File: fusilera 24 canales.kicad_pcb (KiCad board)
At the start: 4 copper layers, 53 parts, among them J1 +12V borne M6, J2 GND borne M5, Q1 MMBT2222A, Q2 MMBT2222A, U1 LM339D, U2 74HC132D, U3 BTS50010-1TAD, U4 MCP23017-E/SO, U5 MCP23017-E/SO, U6 LM5164DDA, U7 AP2112K-3.3

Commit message: Convierte los canales en una hoja jerárquica de celda con dos instancias
- Nueva hoja celda4.kicad_sch (4 canales, 1 LM339 y 2 × 74HC132) instanciada
  como Celda1 y Celda2 en la hoja principal; las referencias de la Celda2 son
  las de la Celda1 más 100.
- Etiquetas únicas por canal como pines de hoja (ESP32_OUT1-4, MANUAL1-4,
  OUT1-4, FALLA1-4): ya no se unen entre sí las salidas, las entradas ni las
  fallas de distintos canales.
- Añade los pull-ups de 10 k que faltaban en las salidas de los comparadores de
  los canales 3 y 4 (R53 y R54).
- Re-vincula en el PCB los 25 footprints existentes de la celda a la Celda1 para
  conservar su colocación.
- La huella de la ESP32 lleva los nombres de los pines en la serigrafía.
- CONTEXTO_PROYECTO.md actualizado: 28 canales (19 controlados y 9 siempre en
  alto), reparto de E/S sin tercer MCP y estructura jerárquica.
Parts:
- added C101: 100uF 16V, Capacitor_SMD:CP_Elec_6.3x5.4, F.Cu at (42.5, 148.8)
- added C102: 100nF, Capacitor_SMD:C_0805_2012Metric, F.Cu at (72.4, 130.0)
- added C103: 1uF 25V, Capacitor_SMD:CP_Elec_4x5.4, F.Cu at (41.1, 102.2)
- added C104: 100nF, Capacitor_SMD:C_0805_2012Metric, F.Cu at (72.4, 133.0)
- added C105: 1uF 25V, Capacitor_SMD:CP_Elec_4x5.4, F.Cu at (41.1, 108.0)
- added C116: 1uF 25V, Capacitor_SMD:CP_Elec_4x5.4, F.Cu at (41.1, 113.9)
- added C117: 1uF 25V, Capacitor_SMD:CP_Elec_4x5.4, F.Cu at (41.1, 119.7)
- added C118: 1uF 25V, Capacitor_SMD:CP_Elec_4x5.4, F.Cu at (41.1, 125.6)
- added C119: 1uF 25V, Capacitor_SMD:CP_Elec_4x5.4, F.Cu at (48.8, 102.2)
- added C120: 100nF, Capacitor_SMD:C_0805_2012Metric, F.Cu at (72.4, 136.0)
- added C121: 1uF 25V, Capacitor_SMD:CP_Elec_4x5.4, F.Cu at (48.8, 108.0)
- added C122: 1uF 25V, Capacitor_SMD:CP_Elec_4x5.4, F.Cu at (48.8, 113.9)
- added C16: 1uF 25V, Capacitor_SMD:CP_Elec_4x5.4, F.Cu at (41.1, 157.8)
- added C17: 1uF 25V, Capacitor_SMD:CP_Elec_4x5.4, F.Cu at (41.1, 163.6)
- added C18: 1uF 25V, Capacitor_SMD:CP_Elec_4x5.4, F.Cu at (41.1, 169.5)
- added C19: 1uF 25V, Capacitor_SMD:CP_Elec_4x5.4, F.Cu at (41.1, 175.3)
- added C20: 100nF, Capacitor_SMD:C_0805_2012Metric, F.Cu at (47.2, 196.3)
- added C21: 1uF 25V, Capacitor_SMD:CP_Elec_4x5.4, F.Cu at (41.1, 181.2)
- added C22: 1uF 25V, Capacitor_SMD:CP_Elec_4x5.4, F.Cu at (41.1, 187.0)
- added D10: LED rojo, LED_SMD:LED_0805_2012Metric, F.Cu at (64.8, 162.4)
- added D101: BAT54C, Package_TO_SOT_SMD:SOT-23, F.Cu at (53.0, 130.7)
- added D102: LED verde, LED_SMD:LED_0805_2012Metric, F.Cu at (77.0, 100.8)
- added D103: LED rojo, LED_SMD:LED_0805_2012Metric, F.Cu at (77.0, 103.8)
- added D107: LED verde, LED_SMD:LED_0805_2012Metric, F.Cu at (77.0, 106.8)
- added D108: BAT54C, Package_TO_SOT_SMD:SOT-23, F.Cu at (53.0, 135.2)
- added D109: LED rojo, LED_SMD:LED_0805_2012Metric, F.Cu at (77.0, 109.9)
- added D11: LED rojo, LED_SMD:LED_0805_2012Metric, F.Cu at (64.8, 165.5)
- added D110: LED rojo, LED_SMD:LED_0805_2012Metric, F.Cu at (77.0, 112.9)
- added D111: LED rojo, LED_SMD:LED_0805_2012Metric, F.Cu at (77.0, 116.0)
- added D112: LED verde, LED_SMD:LED_0805_2012Metric, F.Cu at (77.0, 119.0)
- added D113: LED verde, LED_SMD:LED_0805_2012Metric, F.Cu at (77.0, 122.0)
- added D114: BAT54C, Package_TO_SOT_SMD:SOT-23, F.Cu at (53.0, 139.6)
- added D115: BAT54C, Package_TO_SOT_SMD:SOT-23, F.Cu at (57.9, 130.7)
- added D12: LED verde, LED_SMD:LED_0805_2012Metric, F.Cu at (64.8, 168.5)
- added D13: LED verde, LED_SMD:LED_0805_2012Metric, F.Cu at (64.8, 171.6)
- added D14: BAT54C, Package_TO_SOT_SMD:SOT-23, F.Cu at (47.4, 188.1)
- added D15: BAT54C, Package_TO_SOT_SMD:SOT-23, F.Cu at (47.4, 192.5)
- added D7: LED verde, LED_SMD:LED_0805_2012Metric, F.Cu at (64.8, 156.4)
- added D8: BAT54C, Package_TO_SOT_SMD:SOT-23, F.Cu at (47.4, 183.6)
- added D9: LED rojo, LED_SMD:LED_0805_2012Metric, F.Cu at (64.8, 159.4)
- added Q101: MMBT2222A, Package_TO_SOT_SMD:SOT-23, F.Cu at (57.9, 135.2)
- added Q102: MMBT2222A, Package_TO_SOT_SMD:SOT-23, F.Cu at (57.9, 139.6)
- added Q103: MMBT2222A, Package_TO_SOT_SMD:SOT-23, F.Cu at (62.8, 130.7)
- added Q104: MMBT2222A, Package_TO_SOT_SMD:SOT-23, F.Cu at (62.8, 135.2)
- added Q105: MMBT2222A, Package_TO_SOT_SMD:SOT-23, F.Cu at (62.8, 139.6)
- added Q106: MMBT2222A, Package_TO_SOT_SMD:SOT-23, F.Cu at (67.7, 130.7)
- added Q107: MMBT2222A, Package_TO_SOT_SMD:SOT-23, F.Cu at (67.7, 135.2)
- added Q108: MMBT2222A, Package_TO_SOT_SMD:SOT-23, F.Cu at (67.7, 139.6)
- added Q3: MMBT2222A, Package_TO_SOT_SMD:SOT-23, F.Cu at (52.3, 183.6)
- added Q4: MMBT2222A, Package_TO_SOT_SMD:SOT-23, F.Cu at (52.3, 188.1)
- added Q5: MMBT2222A, Package_TO_SOT_SMD:SOT-23, F.Cu at (52.3, 192.5)
- added Q6: MMBT2222A, Package_TO_SOT_SMD:SOT-23, F.Cu at (57.2, 183.6)
- added Q7: MMBT2222A, Package_TO_SOT_SMD:SOT-23, F.Cu at (57.2, 188.1)
- added Q8: MMBT2222A, Package_TO_SOT_SMD:SOT-23, F.Cu at (57.2, 192.5)
- added R101: umbral, Resistor_THT:R_Axial_DIN0207_L6.3mm_D2.5mm_P10.16mm_Horizontal, F.Cu at (38.8, 130.5)
- added R102: 10k, Resistor_SMD:R_0805_2012Metric, F.Cu at (54.9, 100.7)
- added R103: 10k, Resistor_SMD:R_0805_2012Metric, F.Cu at (54.9, 103.7)
- added R104: 4.7k, Resistor_SMD:R_0805_2012Metric, F.Cu at (54.9, 106.6)
- added R105: 4.7k, Resistor_SMD:R_0805_2012Metric, F.Cu at (54.9, 109.6)
- added R106: 10k, Resistor_SMD:R_0805_2012Metric, F.Cu at (54.9, 112.5)
- added R107: 100k, Resistor_SMD:R_0805_2012Metric, F.Cu at (54.9, 115.5)
- added R108: 100k, Resistor_SMD:R_0805_2012Metric, F.Cu at (54.9, 118.4)
- added R109: 1k, Resistor_SMD:R_0805_2012Metric, F.Cu at (54.9, 121.4)
- added R110: 2.2k, Resistor_SMD:R_0805_2012Metric, F.Cu at (54.9, 124.3)
- added R111: 4.7k, Resistor_SMD:R_0805_2012Metric, F.Cu at (59.3, 100.7)
- added R112: 1k, Resistor_SMD:R_0805_2012Metric, F.Cu at (59.3, 103.7)
- added R119: 4.7k, Resistor_SMD:R_0805_2012Metric, F.Cu at (59.3, 106.6)
- added R120: 4.7k, Resistor_SMD:R_0805_2012Metric, F.Cu at (59.3, 109.6)
- added R121: 2.2k, Resistor_SMD:R_0805_2012Metric, F.Cu at (59.3, 112.5)
- added R122: 100k, Resistor_SMD:R_0805_2012Metric, F.Cu at (59.3, 115.5)
- added R123: 100k, Resistor_SMD:R_0805_2012Metric, F.Cu at (59.3, 118.4)
- added R124: 1k, Resistor_SMD:R_0805_2012Metric, F.Cu at (59.3, 121.4)
- added R125: 1k, Resistor_SMD:R_0805_2012Metric, F.Cu at (59.3, 124.3)
- added R126: 4.7k, Resistor_SMD:R_0805_2012Metric, F.Cu at (63.7, 100.7)
- added R127: 10k, Resistor_SMD:R_0805_2012Metric, F.Cu at (63.7, 103.7)
- added R128: 10k, Resistor_SMD:R_0805_2012Metric, F.Cu at (63.7, 106.6)
- added R129: umbral, Resistor_THT:R_Axial_DIN0207_L6.3mm_D2.5mm_P10.16mm_Horizontal, F.Cu at (38.8, 134.6)
- added R130: 10k, Resistor_SMD:R_0805_2012Metric, F.Cu at (63.7, 109.6)
- added R131: 10k, Resistor_SMD:R_0805_2012Metric, F.Cu at (63.7, 112.5)
- added R132: 10k, Resistor_SMD:R_0805_2012Metric, F.Cu at (63.7, 115.5)
- added R133: 1k, Resistor_SMD:R_0805_2012Metric, F.Cu at (63.7, 118.4)
- added R134: 1k, Resistor_SMD:R_0805_2012Metric, F.Cu at (63.7, 121.4)
- added R135: 4.7k, Resistor_SMD:R_0805_2012Metric, F.Cu at (63.7, 124.3)
- added R136: 4.7k, Resistor_SMD:R_0805_2012Metric, F.Cu at (68.1, 100.7)
- added R137: 4.7k, Resistor_SMD:R_0805_2012Metric, F.Cu at (68.1, 103.7)
- added R138: 4.7k, Resistor_SMD:R_0805_2012Metric, F.Cu at (68.1, 106.6)
- added R139: 4.7k, Resistor_SMD:R_0805_2012Metric, F.Cu at (68.1, 109.6)
- added R140: 4.7k, Resistor_SMD:R_0805_2012Metric, F.Cu at (68.1, 112.5)
- added R141: 2.2k, Resistor_SMD:R_0805_2012Metric, F.Cu at (68.1, 115.5)
- added R142: 2.2k, Resistor_SMD:R_0805_2012Metric, F.Cu at (68.1, 118.4)
- added R143: 100k, Resistor_SMD:R_0805_2012Metric, F.Cu at (68.1, 121.4)
- added R144: 100k, Resistor_SMD:R_0805_2012Metric, F.Cu at (68.1, 124.3)
- added R145: 100k, Resistor_SMD:R_0805_2012Metric, F.Cu at (72.5, 100.7)
- added R146: 100k, Resistor_SMD:R_0805_2012Metric, F.Cu at (72.5, 103.7)
- added R147: 1k, Resistor_SMD:R_0805_2012Metric, F.Cu at (72.5, 106.6)
- added R148: 1k, Resistor_SMD:R_0805_2012Metric, F.Cu at (72.5, 109.6)
- added R149: umbral, Resistor_THT:R_Axial_DIN0207_L6.3mm_D2.5mm_P10.16mm_Horizontal, F.Cu at (38.8, 138.6)
- added R150: 10k, Resistor_SMD:R_0805_2012Metric, F.Cu at (72.5, 112.5)
- added R151: umbral, Resistor_THT:R_Axial_DIN0207_L6.3mm_D2.5mm_P10.16mm_Horizontal, F.Cu at (38.8, 142.7)
- added R152: 10k, Resistor_SMD:R_0805_2012Metric, F.Cu at (72.5, 115.5)
- added R153: 10k, Resistor_SMD:R_0805_2012Metric, F.Cu at (72.5, 118.4)
- added R154: 10k, Resistor_SMD:R_0805_2012Metric, F.Cu at (72.5, 121.4)
- added R19: 4.7k, Resistor_SMD:R_0805_2012Metric, F.Cu at (47.2, 156.3)
- added R20: 4.7k, Resistor_SMD:R_0805_2012Metric, F.Cu at (47.2, 159.3)
- added R21: 2.2k, Resistor_SMD:R_0805_2012Metric, F.Cu at (47.2, 162.2)
- added R22: 100k, Resistor_SMD:R_0805_2012Metric, F.Cu at (47.2, 165.2)
- added R23: 100k, Resistor_SMD:R_0805_2012Metric, F.Cu at (47.2, 168.1)
- added R24: 1k, Resistor_SMD:R_0805_2012Metric, F.Cu at (47.2, 171.1)
- added R25: 1k, Resistor_SMD:R_0805_2012Metric, F.Cu at (47.2, 174.0)
- added R26: 4.7k, Resistor_SMD:R_0805_2012Metric, F.Cu at (47.2, 177.0)
- added R27: 10k, Resistor_SMD:R_0805_2012Metric, F.Cu at (47.2, 179.9)
- added R28: 10k, Resistor_SMD:R_0805_2012Metric, F.Cu at (51.6, 156.3)
- added R29: umbral, Resistor_THT:R_Axial_DIN0207_L6.3mm_D2.5mm_P10.16mm_Horizontal, F.Cu at (21.1, 193.9)
- added R30: 10k, Resistor_SMD:R_0805_2012Metric, F.Cu at (51.6, 159.3)
- added R31: 10k, Resistor_SMD:R_0805_2012Metric, F.Cu at (51.6, 162.2)
- added R32: 10k, Resistor_SMD:R_0805_2012Metric, F.Cu at (51.6, 165.2)
- added R33: 1k, Resistor_SMD:R_0805_2012Metric, F.Cu at (51.6, 168.1)
- added R34: 1k, Resistor_SMD:R_0805_2012Metric, F.Cu at (51.6, 171.1)
- added R35: 4.7k, Resistor_SMD:R_0805_2012Metric, F.Cu at (51.6, 174.0)
- added R36: 4.7k, Resistor_SMD:R_0805_2012Metric, F.Cu at (51.6, 177.0)
- added R37: 4.7k, Resistor_SMD:R_0805_2012Metric, F.Cu at (51.6, 179.9)
- added R38: 4.7k, Resistor_SMD:R_0805_2012Metric, F.Cu at (56.0, 156.3)
- added R39: 4.7k, Resistor_SMD:R_0805_2012Metric, F.Cu at (56.0, 159.3)
- added R40: 4.7k, Resistor_SMD:R_0805_2012Metric, F.Cu at (56.0, 162.2)
- added R41: 2.2k, Resistor_SMD:R_0805_2012Metric, F.Cu at (56.0, 165.2)
- added R42: 2.2k, Resistor_SMD:R_0805_2012Metric, F.Cu at (56.0, 168.1)
- added R43: 100k, Resistor_SMD:R_0805_2012Metric, F.Cu at (56.0, 171.1)
- added R44: 100k, Resistor_SMD:R_0805_2012Metric, F.Cu at (56.0, 174.0)
- added R45: 100k, Resistor_SMD:R_0805_2012Metric, F.Cu at (56.0, 177.0)
- added R46: 100k, Resistor_SMD:R_0805_2012Metric, F.Cu at (56.0, 179.9)
- added R47: 1k, Resistor_SMD:R_0805_2012Metric, F.Cu at (60.4, 156.3)
- added R48: 1k, Resistor_SMD:R_0805_2012Metric, F.Cu at (60.4, 159.3)
- added R49: umbral, Resistor_THT:R_Axial_DIN0207_L6.3mm_D2.5mm_P10.16mm_Horizontal, F.Cu at (21.1, 198.0)
- added R50: 10k, Resistor_SMD:R_0805_2012Metric, F.Cu at (60.4, 162.2)
- added R51: umbral, Resistor_THT:R_Axial_DIN0207_L6.3mm_D2.5mm_P10.16mm_Horizontal, F.Cu at (21.1, 202.0)
- added R52: 10k, Resistor_SMD:R_0805_2012Metric, F.Cu at (60.4, 165.2)
- added R53: 10k, Resistor_SMD:R_0805_2012Metric, F.Cu at (60.4, 168.1)
- added R54: 10k, Resistor_SMD:R_0805_2012Metric, F.Cu at (60.4, 171.1)
- added U10: BTS50010-1TAD, Package_TO_SOT_SMD:TO-263-7_TabPin4, F.Cu at (30.2, 173.4)
- added U101: LM339D, Package_SO:SOIC-14_3.9x8.7mm_P1.27mm, F.Cu at (54.7, 147.1)
- added U102: 74HC132D, Package_SO:SOIC-14_3.9x8.7mm_P1.27mm, F.Cu at (63.2, 147.1)
- added U103: BTS50010-1TAD, Package_TO_SOT_SMD:TO-263-7_TabPin4, F.Cu at (30.2, 105.4)
- added U108: BTS50010-1TAD, Package_TO_SOT_SMD:TO-263-7_TabPin4, F.Cu at (30.2, 117.8)
- added U109: 74HC132D, Package_SO:SOIC-14_3.9x8.7mm_P1.27mm, F.Cu at (71.6, 147.1)
- added U11: BTS50010-1TAD, Package_TO_SOT_SMD:TO-263-7_TabPin4, F.Cu at (30.2, 185.7)
- added U110: BTS50010-1TAD, Package_TO_SOT_SMD:TO-263-7_TabPin4, F.Cu at (30.2, 130.1)
- added U111: BTS50010-1TAD, Package_TO_SOT_SMD:TO-263-7_TabPin4, F.Cu at (30.2, 142.5)
- added U8: BTS50010-1TAD, Package_TO_SOT_SMD:TO-263-7_TabPin4, F.Cu at (30.2, 161.0)
- added U9: 74HC132D, Package_SO:SOIC-14_3.9x8.7mm_P1.27mm, F.Cu at (63.9, 186.7)
- moved A1 110.6 mm to (121.8, 63.0)
- moved U3 82.2 mm to (184.7, 63.7)
- moved R1 53.5 mm to (15.2, 32.0)
- moved U1 29.9 mm to (34.8, 34.5)
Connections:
- net /ESP32 OUT renamed /Celda1/ESP32_OUT1
- net /MANUAL renamed /Celda1/MANUAL1
- net /OUT renamed /Celda1/OUT1
- net /U2A-3 renamed Net-(U2-Pad3)
- net U2A-2 renamed /Celda1/FALLA1
- net U2B-4 renamed Net-(R3-Pad1)
- net U3-IN renamed Net-(Q2-C)
- net U3-IS renamed Net-(U1A--)
- U1 pad 1: unconnected-(U1-Pad1) -> Net-(R27-Pad1)
- U1 pad 10: unconnected-(U1C---Pad10) -> Net-(U10-IS)
- U1 pad 11: unconnected-(U1C-+-Pad11) -> Net-(U1C-+)
- U1 pad 13: unconnected-(U1-Pad13) -> Net-(R53-Pad1)
- U1 pad 14: unconnected-(U1-Pad14) -> Net-(R54-Pad1)
- U1 pad 6: unconnected-(U1B---Pad6) -> Net-(U1B--)
- U1 pad 7: unconnected-(U1B-+-Pad7) -> Net-(U1B-+)
- U1 pad 8: unconnected-(U1D---Pad8) -> Net-(U11-IS)
- U1 pad 9: unconnected-(U1D-+-Pad9) -> Net-(U1D-+)
- U2 pad 10: unconnected-(U2-Pad10) -> /Celda1/FALLA2
- U2 pad 11: unconnected-(U2-Pad11) -> /Celda1/FALLA2
- U2 pad 12: unconnected-(U2-Pad12) -> Net-(R27-Pad1)
- U2 pad 13: unconnected-(U2-Pad13) -> Net-(U2-Pad13)
- U2 pad 8: unconnected-(U2-Pad8) -> Net-(U2-Pad13)
- U2 pad 9: unconnected-(U2-Pad9) -> Net-(C17-Pad1)

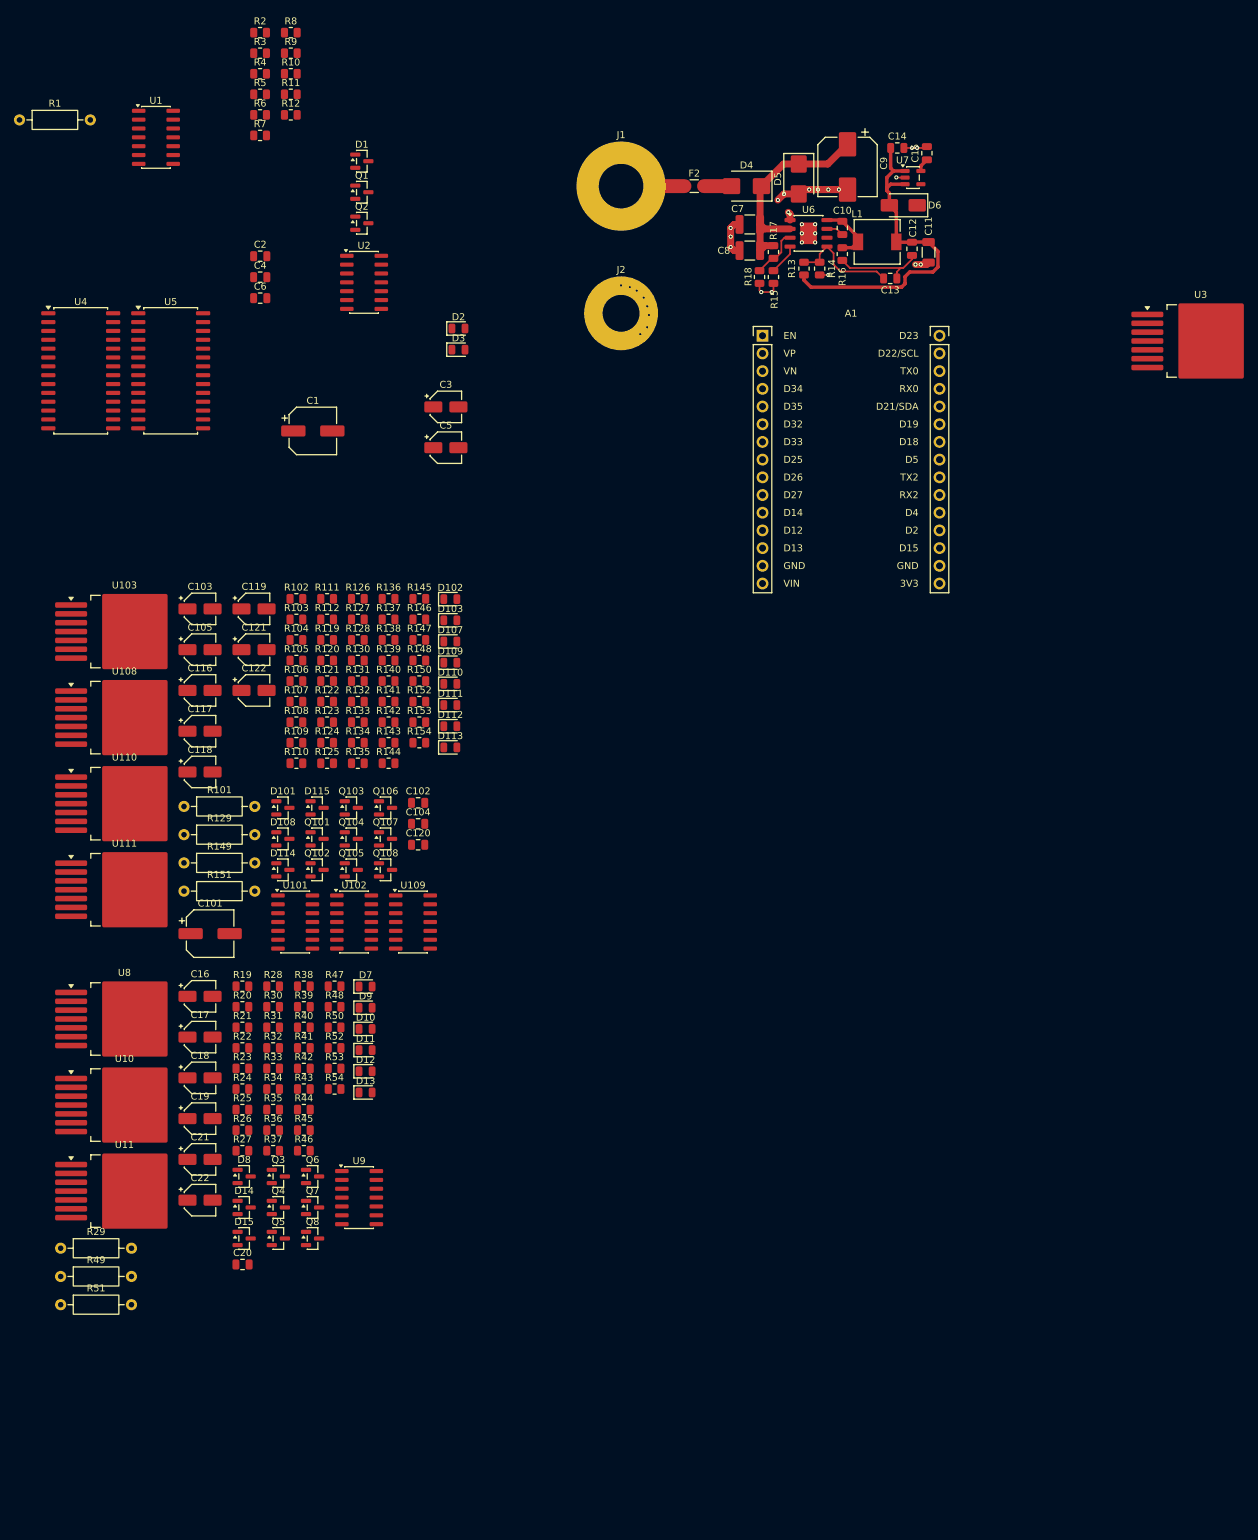
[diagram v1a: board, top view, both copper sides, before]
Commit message: Importa las dos celdas al PCB y avanza el ruteo de la Celda1
- Importa a la placa los 202 footprints (bloque de alimentación, ESP32, MCP23017
  y las celdas Celda1 y Celda2); paridad con el esquemático sin problemas.
- Avanza el ruteo: 371 segmentos y 43 vías; el plano de GND de In1 se mantiene.
- Reubica en el esquemático el grupo del ESP32 y los MCP23017.
- El DRC sigue marcando el contorno que falta, 260 conexiones por rutear y
  18 avisos de espaciado pendientes de revisar.
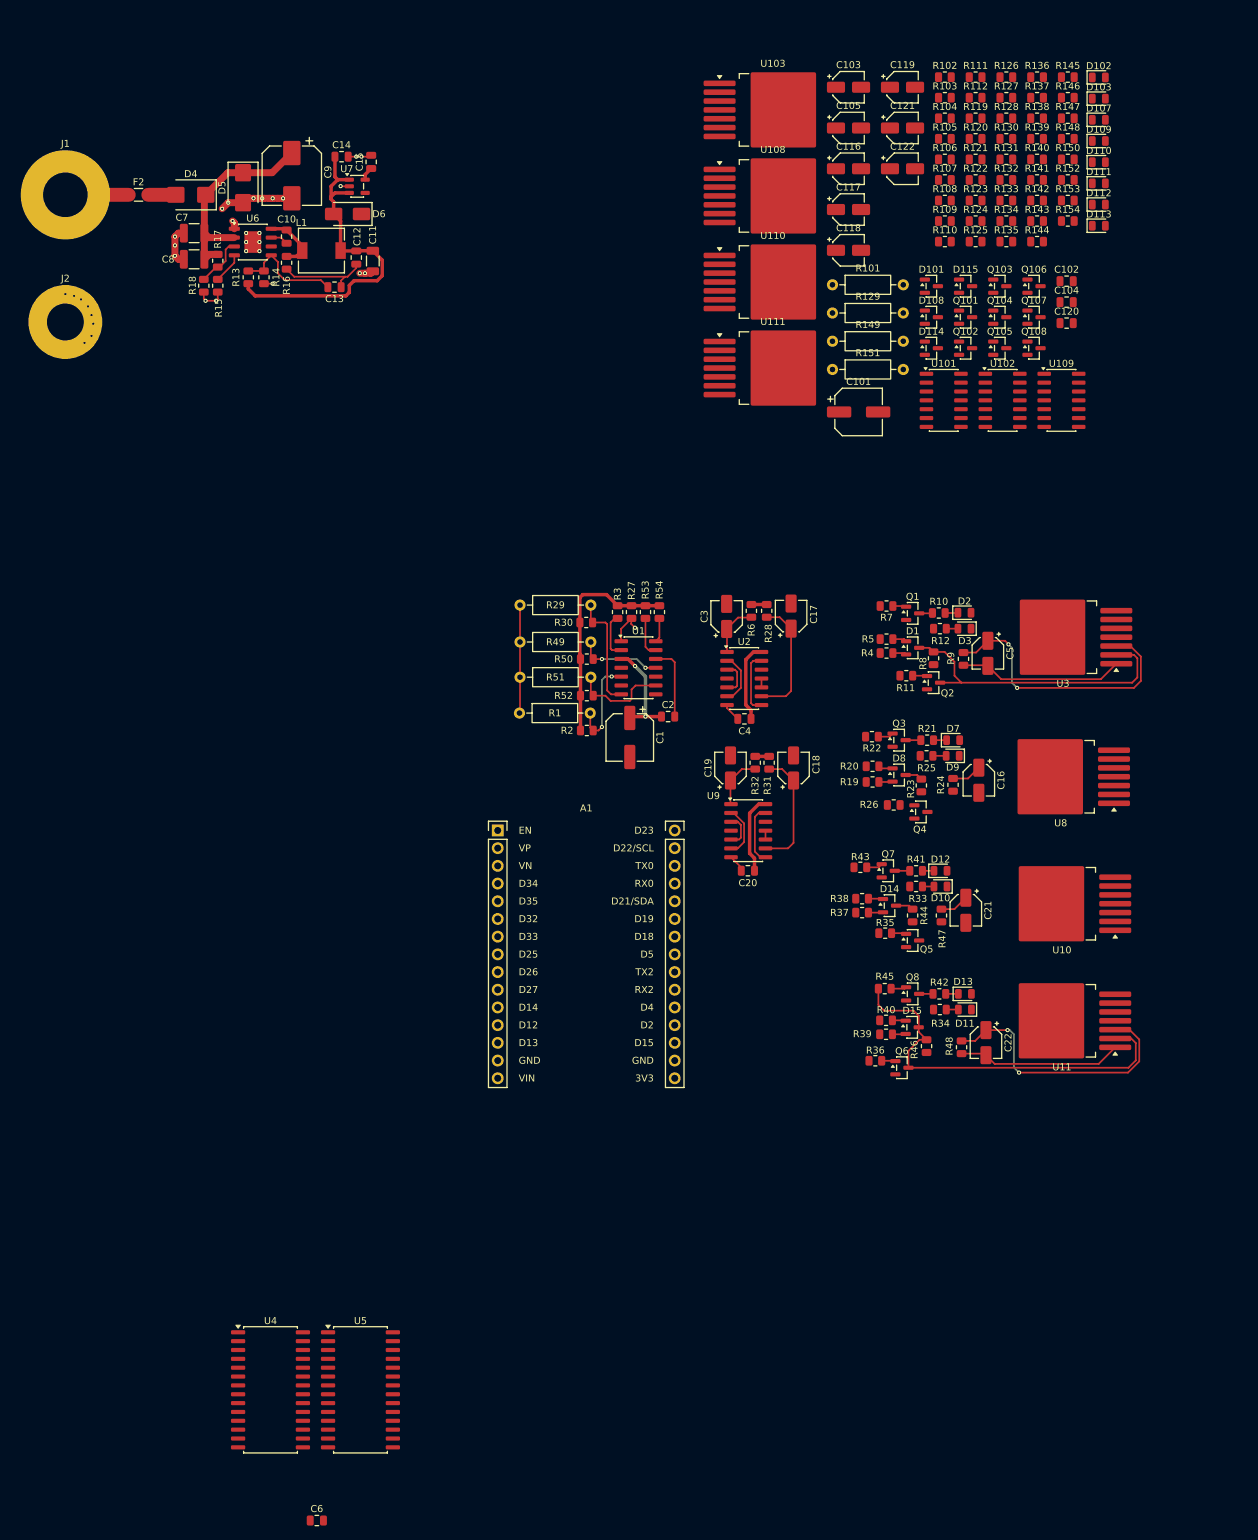
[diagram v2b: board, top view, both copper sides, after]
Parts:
- moved C6 175.6 mm to (57.8, 233.0)
- moved U4 148.8 mm to (51.2, 214.2)
- moved U5 148.8 mm to (64.1, 214.2)
- moved U8 138.8 mm to (164.6, 126.3), turned to 180 degrees
- moved U10 137.6 mm to (164.8, 144.5), turned to 180 degrees
- moved U11 136.7 mm to (164.8, 161.3), turned to 180 degrees
- moved R9 129.9 mm to (150.6, 109.3), turned to -90 degrees
- moved R8 128.7 mm to (146.3, 109.3), turned to -90 degrees
- moved R4 122.4 mm to (139.6, 108.5)
- moved R11 121.5 mm to (142.4, 111.8), turned to 180 degrees
- moved R10 121.0 mm to (147.1, 102.8)
- moved R148 119.4 mm to (165.6, 34.7)
- moved R150 119.4 mm to (165.6, 37.7)
- moved R154 119.4 mm to (165.6, 46.5)
- moved U101 119.4 mm to (147.8, 72.2)
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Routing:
- net GND: track 0.00 -> 79.0 mm
- net +3.3V: track 0.00 -> 73.3 mm, vias 0 -> 2
- net Net-(Q6-C): track 0.00 -> 57.2 mm
- net Net-(Q2-C): track 0.00 -> 43.9 mm
- net Net-(U1A--): track 0.00 -> 40.0 mm, vias 0 -> 2
- net Net-(U11-IS): track 0.00 -> 39.3 mm, vias 0 -> 2
- net Net-(C17-Pad1): track 0.00 -> 17.7 mm
- net Net-(C18-Pad1): track 0.00 -> 17.5 mm
- net Net-(U1B-+): track 0.00 -> 16.6 mm
- net Net-(U1A-+): track 0.00 -> 13.9 mm, vias 0 -> 2
- net Net-(U1D-+): track 0.00 -> 13.8 mm
- net Net-(U1C-+): track 0.00 -> 12.1 mm, vias 0 -> 2
- net Net-(U2-Pad13): track 0.00 -> 9.00 mm
- net Net-(U9-Pad13): track 0.00 -> 8.60 mm
- net Net-(C19-Pad1): track 0.00 -> 7.65 mm
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
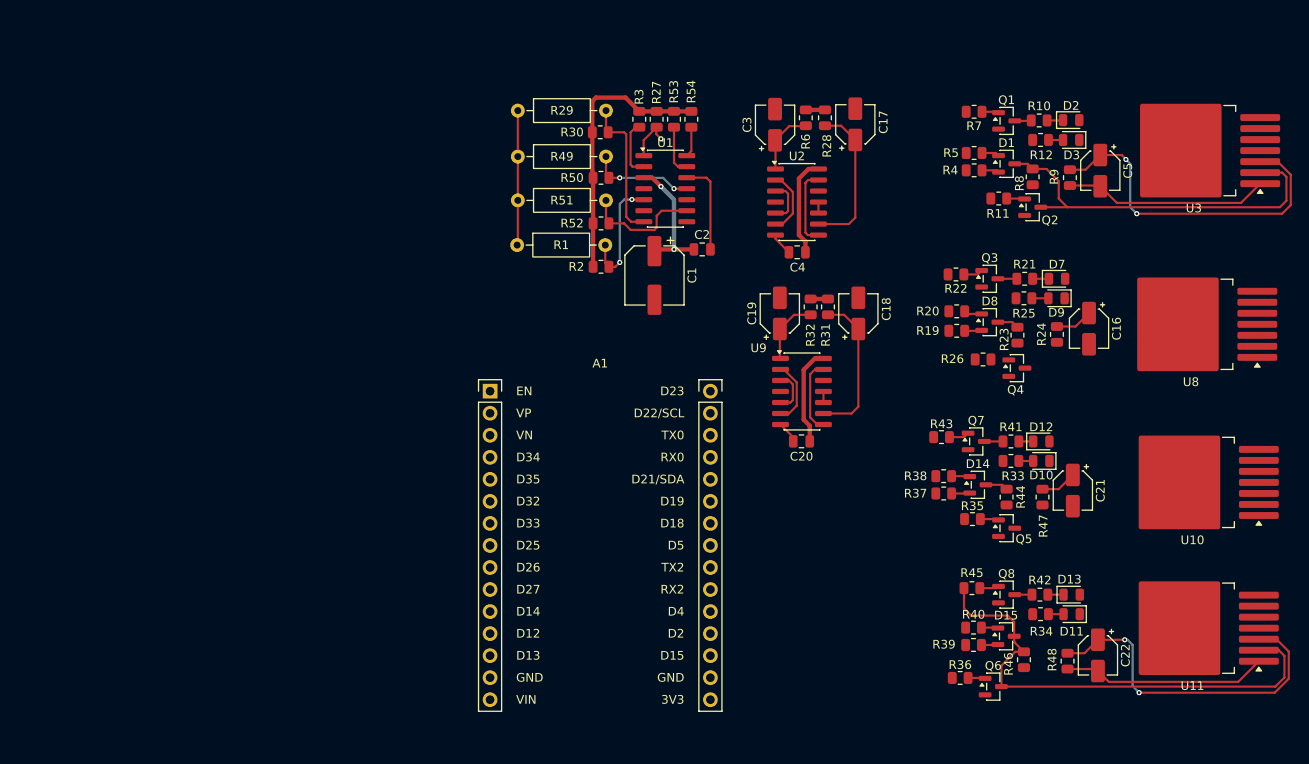
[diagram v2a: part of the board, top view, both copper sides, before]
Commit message: Avanza el ruteo de la Celda1 y rehace el plano de GND sobre ella
Rutea parte de IN/IS en In2, mueve la Celda2 a su propia zona y redibuja el
plano de GND de In1 para cubrir la Celda1. El plano ya no cubre el bloque de
poder, por lo que sus vías de GND quedan pendientes de un plano que las una.
Se actualiza CONTEXTO_PROYECTO.md con el estado del PCB.
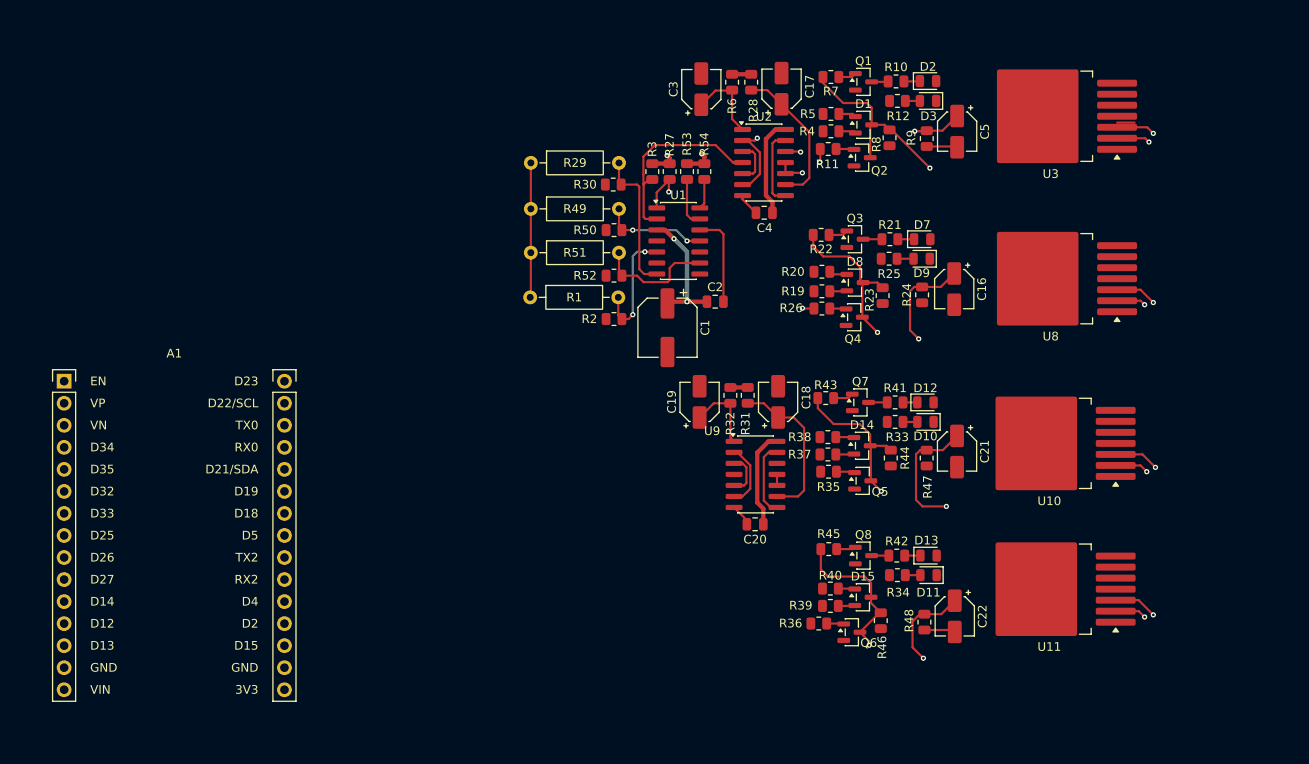
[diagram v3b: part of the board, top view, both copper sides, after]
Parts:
- moved A1 49.1 mm to (34.7, 132.8)
- moved Q2 20.5 mm to (126.7, 107.0)
- moved R11 20.5 mm to (122.8, 106.0)
- moved Q4 19.7 mm to (125.8, 125.4)
- moved R26 19.5 mm to (122.0, 124.4)
- moved Q6 17.5 mm to (125.5, 161.8)
- moved R36 17.5 mm to (121.7, 160.8)
- moved R35 17.5 mm to (122.8, 143.2)
- moved Q5 17.5 mm to (126.8, 144.3)
- moved C22 17.1 mm to (137.4, 159.9)
- moved C5 17.1 mm to (137.6, 104.0)
- moved D1 17.1 mm to (126.8, 103.3)
- moved D11 17.1 mm to (134.3, 155.2)
- moved D13 17.1 mm to (134.3, 152.9)
- moved D15 17.1 mm to (126.8, 157.7)
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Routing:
- net Net-(Q5-C): track 2.58 -> 55.8 mm, vias 0 -> 2
- net Net-(Q4-C): track 2.49 -> 55.6 mm, vias 0 -> 2
- net Net-(U10-IS): track 4.18 -> 47.6 mm, vias 0 -> 2
- net Net-(U1B--): track 4.34 -> 47.0 mm, vias 0 -> 2
- net GND: track 79.0 -> 38.8 mm
- net +3.3V: track 73.3 -> 48.4 mm, vias 2 -> 4
- net Net-(R27-Pad1): track 5.84 -> 27.2 mm, vias 1 -> 2
- net /Celda1/FALLA2: track 1.27 -> 20.2 mm, vias 0 -> 2
- net Net-(R3-Pad1): track 6.61 -> 22.6 mm
- net /Celda1/FALLA1: track 7.57 -> 20.6 mm, vias 0 -> 2
- net Net-(Q2-C): track 43.9 -> 53.7 mm, vias 0 -> 2
- net Net-(U1A--): track 40.0 -> 48.8 mm
- net Net-(U11-IS): track 39.3 -> 45.8 mm
- net Net-(Q4-B): track 0.00 -> 1.90 mm
- net Net-(C3-Pad1): track 7.55 -> 9.33 mm
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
